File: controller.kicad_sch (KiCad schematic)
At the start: 22 parts, among them J1 PH254, J9 M3, U2 TLIN4029A, U8 ATtiny806-S

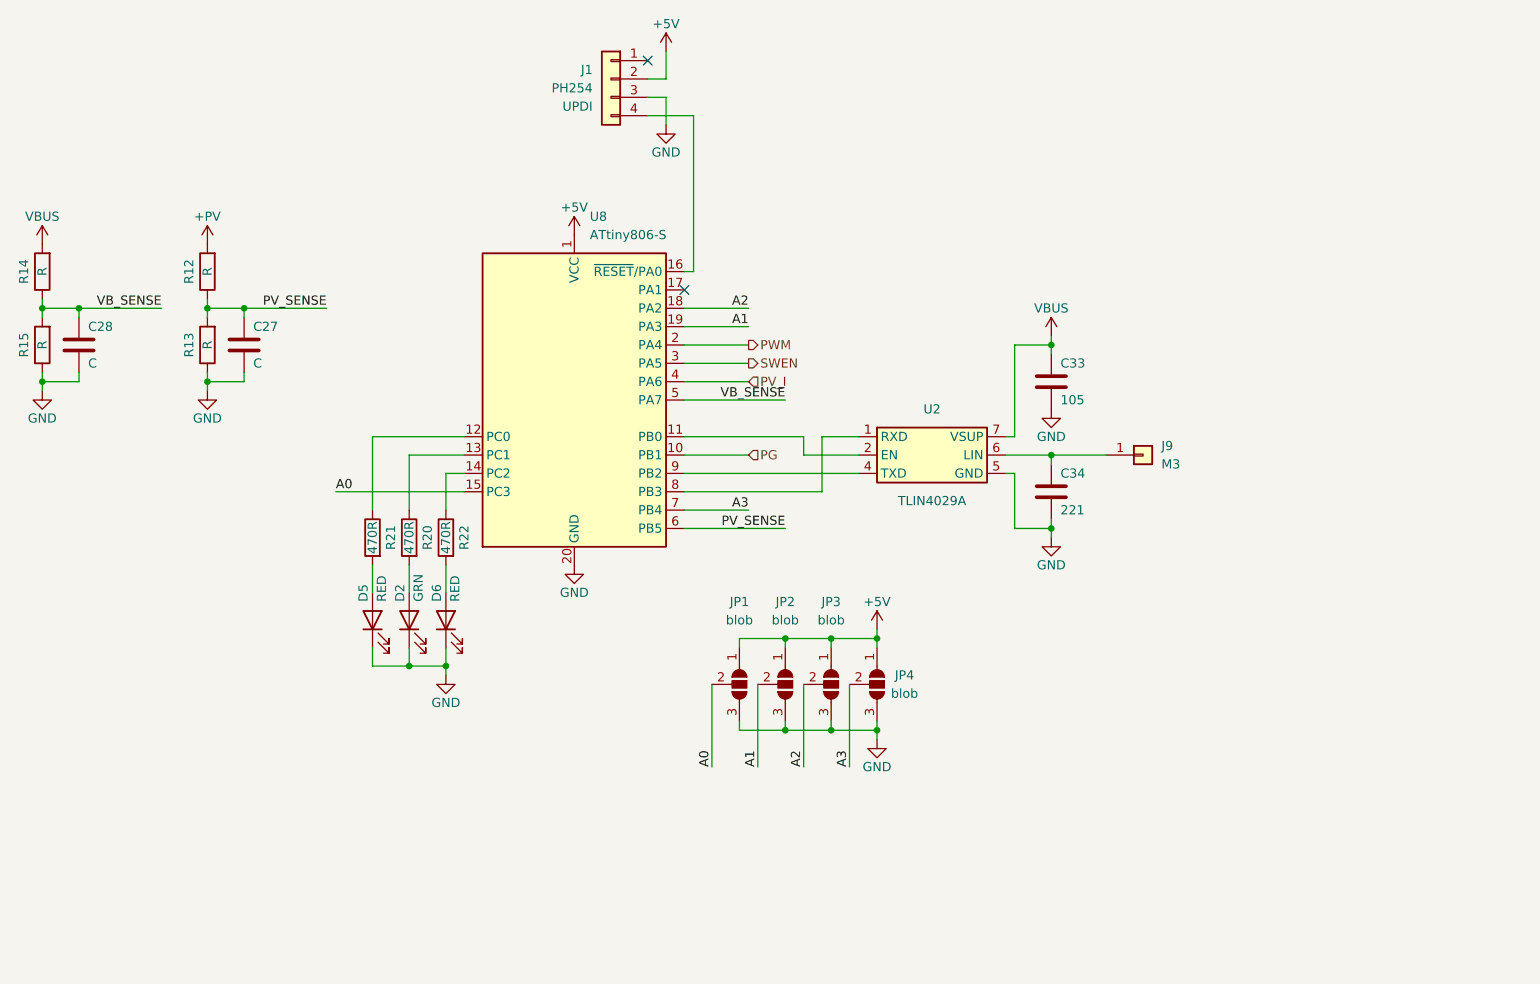
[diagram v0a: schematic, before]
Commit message: Changed MCU to AT90PWM316-16M - much higher PWM frequency than the Atiny. Smaller inductor and replaced electrolytic capacitors with ceramic.
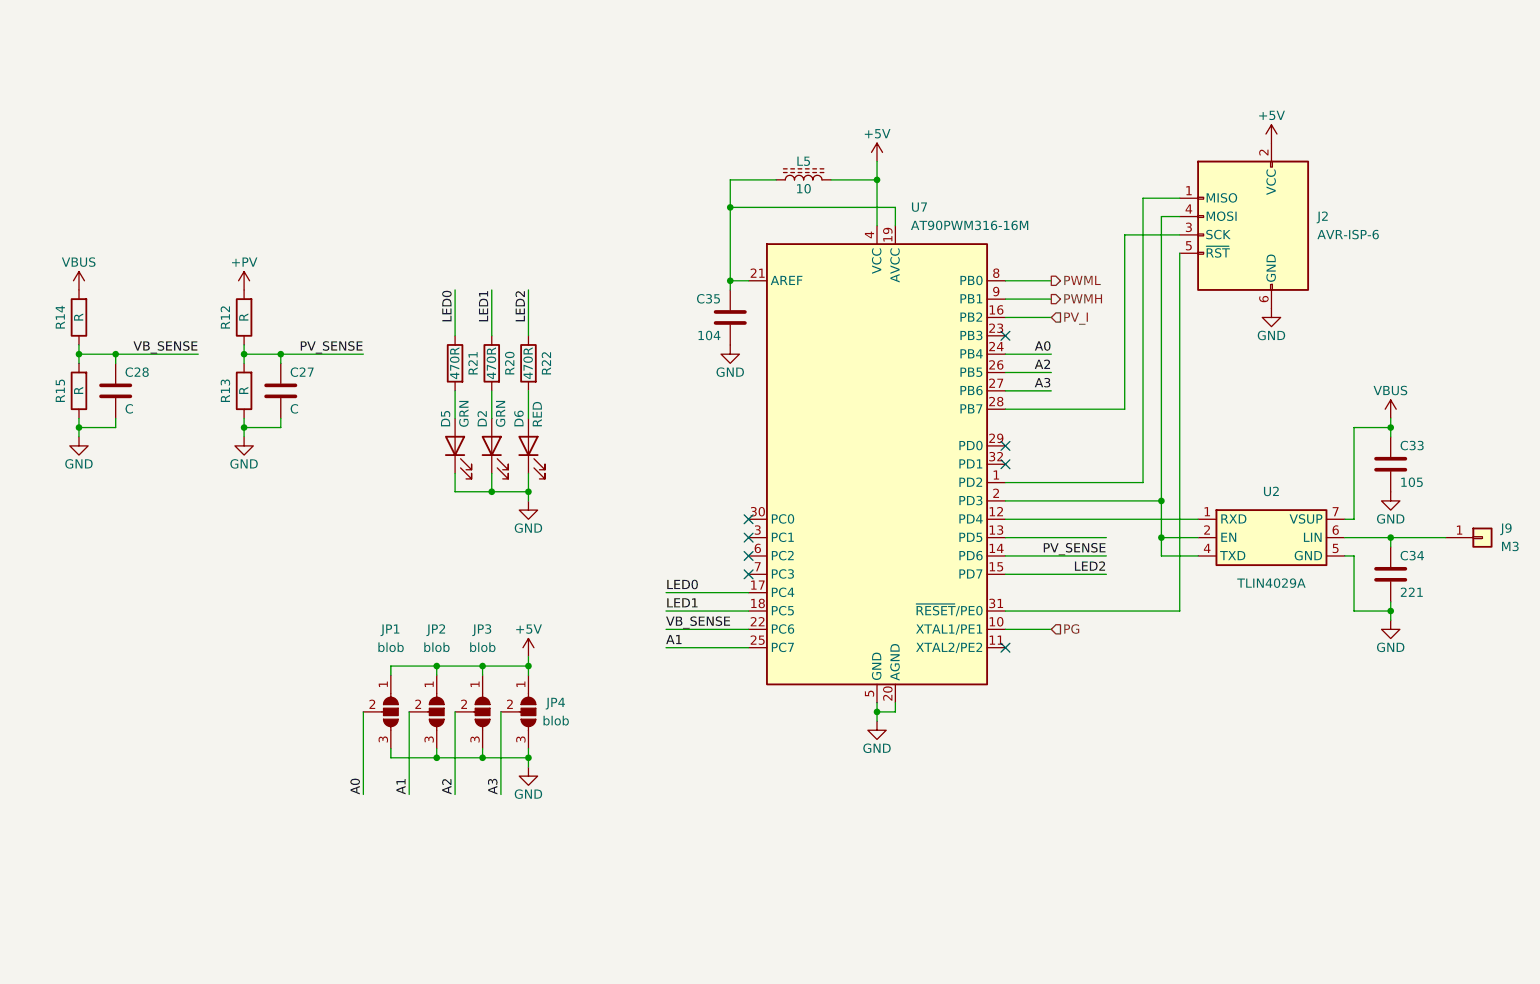
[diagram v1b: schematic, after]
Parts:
- removed J1: PH254, Connector_PinHeader_2.54mm:PinHeader_1x04_P2.54mm_Vertical_SMD_Pin1Left, symbol Connector_Generic:Conn_01x04
- removed U8: ATtiny806-S, Package_SO:SOIC-20W_7.5x12.8mm_P1.27mm, symbol MCU_Microchip_ATtiny:ATtiny806-S
- added C35: 104, Capacitor_SMD:C_0805_2012Metric, symbol Device:C
- added J2: AVR-ISP-6, Connector_PinHeader_2.54mm:PinHeader_2x03_P2.54mm_Vertical_SMD, symbol Connector:AVR-ISP-6
- added L5: 10, Inductor_SMD:L_0805_2012Metric, symbol Device:L_Ferrite
- added U7: AT90PWM316-16M, Package_DFN_QFN:QFN-32-1EP_7x7mm_P0.65mm_EP4.65x4.65mm, symbol HR_parts:AT90PWM316-16M
- D2: Function (none) -> LIN
- D5: value RED -> GRN; Function (none) -> ACT
- D6: Function (none) -> FLT
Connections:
- net +5V: now also J2.2 (VCC), L5.2, U7.4 (VCC)
- net A0: now also U7.24 (PB4)
- net A1: now also U7.25 (PC7)
- net A2: now also U7.26 (PB5)
- net A3: now also U7.27 (PB6)
- net GND: now also C35.2, J2.6 (GND), U7.20 (AGND), U7.33 (GND), U7.5 (GND)
- net PG: now also U7.10 (XTAL1/PE1)
- net PV_I: now also U7.16 (PB2)
- net PV_SENSE: now also U7.14 (PD6)
- net VB_SENSE: now also U7.22 (PC6)
- net LED2: now reaches R22.1
- net LED2: now also U7.15 (PD7)
- net LED1: now reaches R20.1
- net LED1: now also U7.18 (PC5)
- net at U2.2 (EN): now also U2.4 (TXD), J2.4 (MOSI), U7.2 (PD3)
- net LED0: now reaches R21.1
- net LED0: now also U7.17 (PC4)
- net at U2.1 (RXD): now also U7.12 (PD4)
- new net: J2.1 (MISO), U7.1 (PD2)
- new net: C35.1, L5.1, U7.19 (AVCC), U7.21 (AREF)
- new net: J2.3 (SCK), U7.28 (PB7)
- new net: J2.5 (~{RST}), U7.31 (~{RESET}/PE0)
- new net PWMH: U7.9 (PB1)
- new net PWML: U7.8 (PB0)
- no-connect marks 2 -> 8
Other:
- moved on the sheet: C27, C28, C33, C34, D2, D5, D6, J9, JP1, JP2, JP3, JP4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

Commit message: Temperature sensor added as the AT90PWM316 does not have an internal one.
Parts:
- added U1: MCP9700Ax-ETT, Package_TO_SOT_SMD:SOT-23, symbol Sensor_Temperature:MCP9700Ax-ETT
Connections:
- net +5V: now also U1.1 (V_{DD})
- net A0: now also U7.23 (PB3); no longer U7.24 (PB4)
- net A1: now also U7.24 (PB4); no longer U7.25 (PC7)
- net A2: now also U7.25 (PC7); no longer U7.26 (PB5)
- net A3: now also U7.26 (PB5); no longer U7.27 (PB6)
- net GND: now also U1.3 (GND)
- new net TEMP: U1.2 (V_{OUT}), U7.27 (PB6)
- no-connect marks 8 -> 7

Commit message: Missing component values added.
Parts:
- R12, R14: value R -> 24K
- R13, R15: value R -> 1K
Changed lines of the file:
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@@
 			)
 		)
-		(property "Value" "R"
+		(property "Value" "1K"
 			(at 52.07 74.93 90)
 			(show_name no)
@@
 			)
 		)
-		(property "Value" "R"
+		(property "Value" "1K"
 			(at 74.93 74.93 90)
 			(show_name no)
@@
 			)
 		)
-		(property "Value" "R"
+		(property "Value" "24K"
 			(at 74.93 64.77 90)
 			(show_name no)
@@
 			)
 		)
-		(property "Value" "R"
+		(property "Value" "24K"
 			(at 52.07 64.77 90)
 			(show_name no)
